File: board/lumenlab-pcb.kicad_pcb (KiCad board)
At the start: 2 copper layers, 59 parts, among them J1 2.1mm Barrel Jack, J2 Screw_Terminal_01x04, J3 Screw_Terminal_01x06, J4 Conn_01x04_Pin, U1 MP2338, U2 AP7361C-33E, U3 SN74AHC1G125DBVR, U4 1_Custom_LM386MX-1_NOPB, U5 SN74HC14DR, U6 ESP32-WROOM-32E

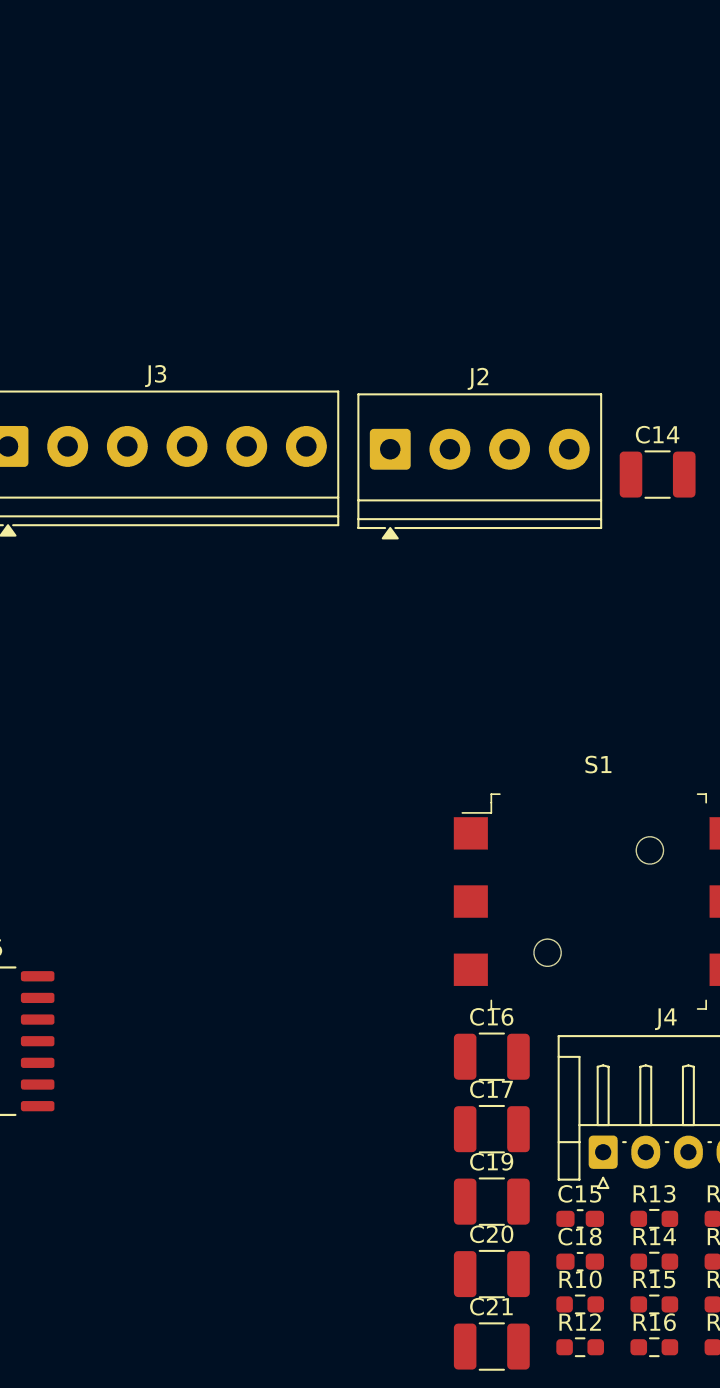
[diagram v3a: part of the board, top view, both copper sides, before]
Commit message: Add JTAG header for code upload
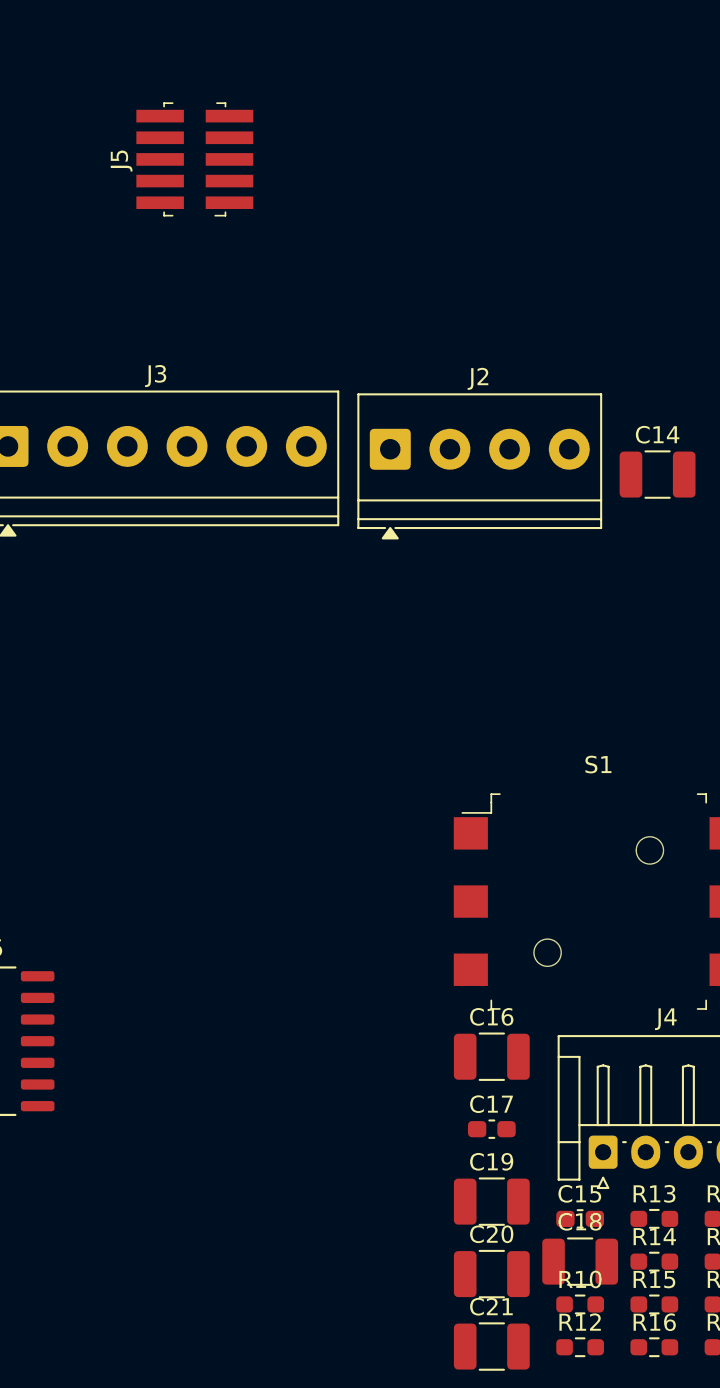
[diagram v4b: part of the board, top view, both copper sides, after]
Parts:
- added J5: JTAG, digikey-footprints:PinHeader_2x5_P1.27_SMD, F.Cu at (180.0, 69.5)
- C11: value 0.1uF -> 22uF
- C12: value 10uF -> 0.1uF
- C17: footprint Capacitor_SMD:C_1210_3225Metric_Pad1.33x2.70mm_HandSolder -> Capacitor_SMD:C_0603_1608Metric_Pad1.08x0.95mm_HandSolder
- C18: footprint Capacitor_SMD:C_0603_1608Metric_Pad1.08x0.95mm_HandSolder -> Capacitor_SMD:C_1210_3225Metric_Pad1.33x2.70mm_HandSolder
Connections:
- C11 pad 1: /DEBOUNCE_UP -> GND
- C11 pad 2: GND -> +3.3V
- C12 pad 1: GND -> +3.3V
- C12 pad 2: +3.3V -> GND
- C14 pad 1: +3.3V -> /DEBOUNCE_UP
- C17 pad 1: /DEBOUNCE_DOWN -> GND
- C17 pad 2: GND -> +3.3V
- C18 pad 1: GND -> /DEBOUNCE_DOWN
- C18 pad 2: +3.3V -> GND
- R18 pad 1: /ESP32_GPIO21 -> /ESP32_GPIO19
- S1 pad 2: GND -> /DEBOUNCE_LEFT
- S1 pad 3: GND -> /DEBOUNCE_PUSH
- S1 pad 4: GND -> /DEBOUNCE_UP
- S1 pad 5: GND -> /DEBOUNCE_RIGHT
- S1 pad 6: GND -> /DEBOUNCE_DOWN
- U6 pad 31: unconnected-(U6-IO19-Pad31) -> /ESP32_GPIO19
- U6 pad 36: unconnected-(U6-IO22-Pad36) -> /ESP32_GPIO22

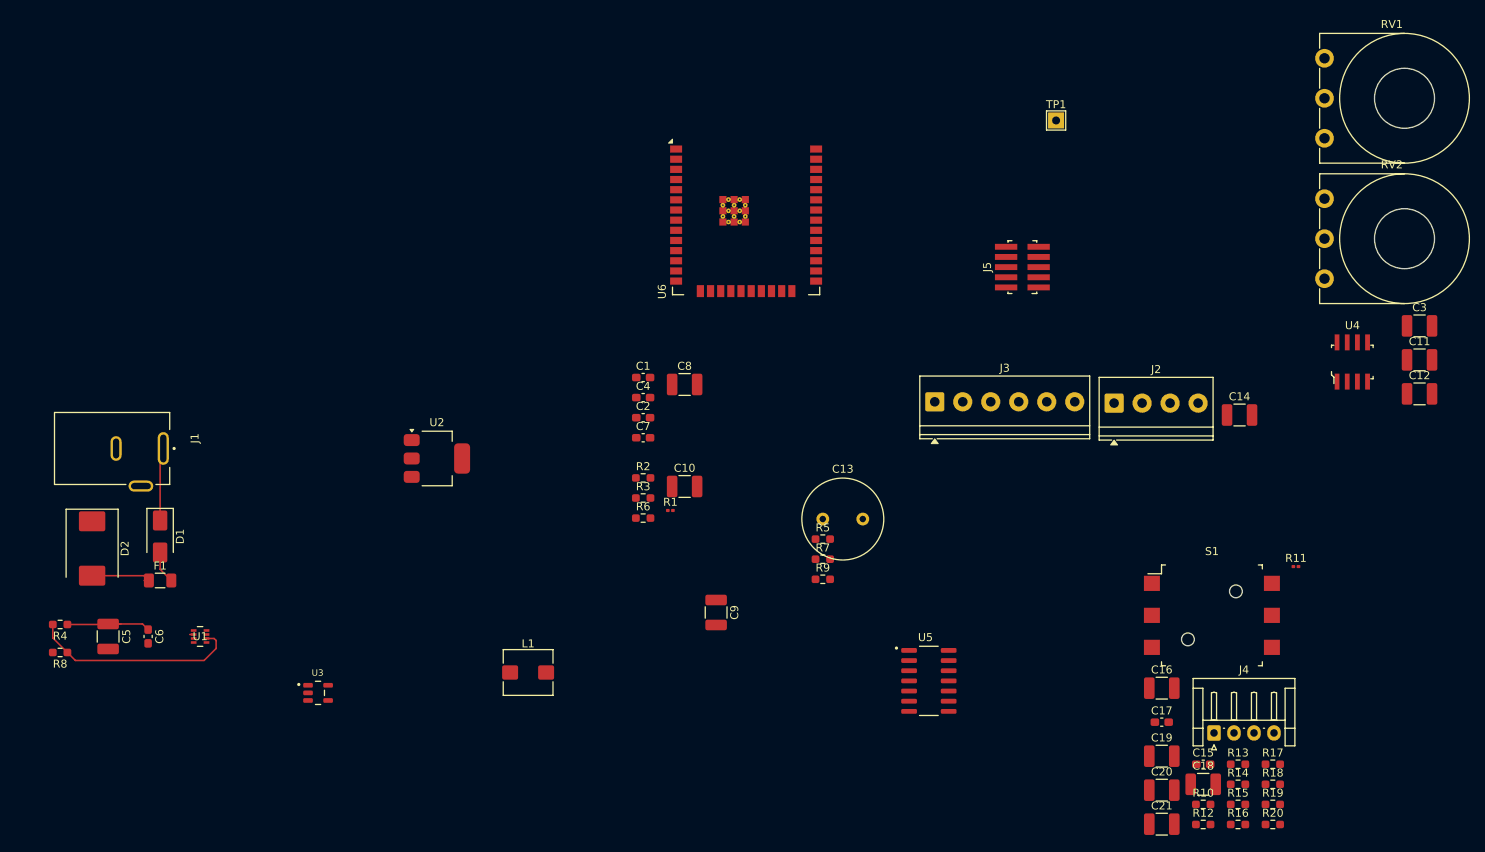
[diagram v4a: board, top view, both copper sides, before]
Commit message: Replace footprints with available components, add models
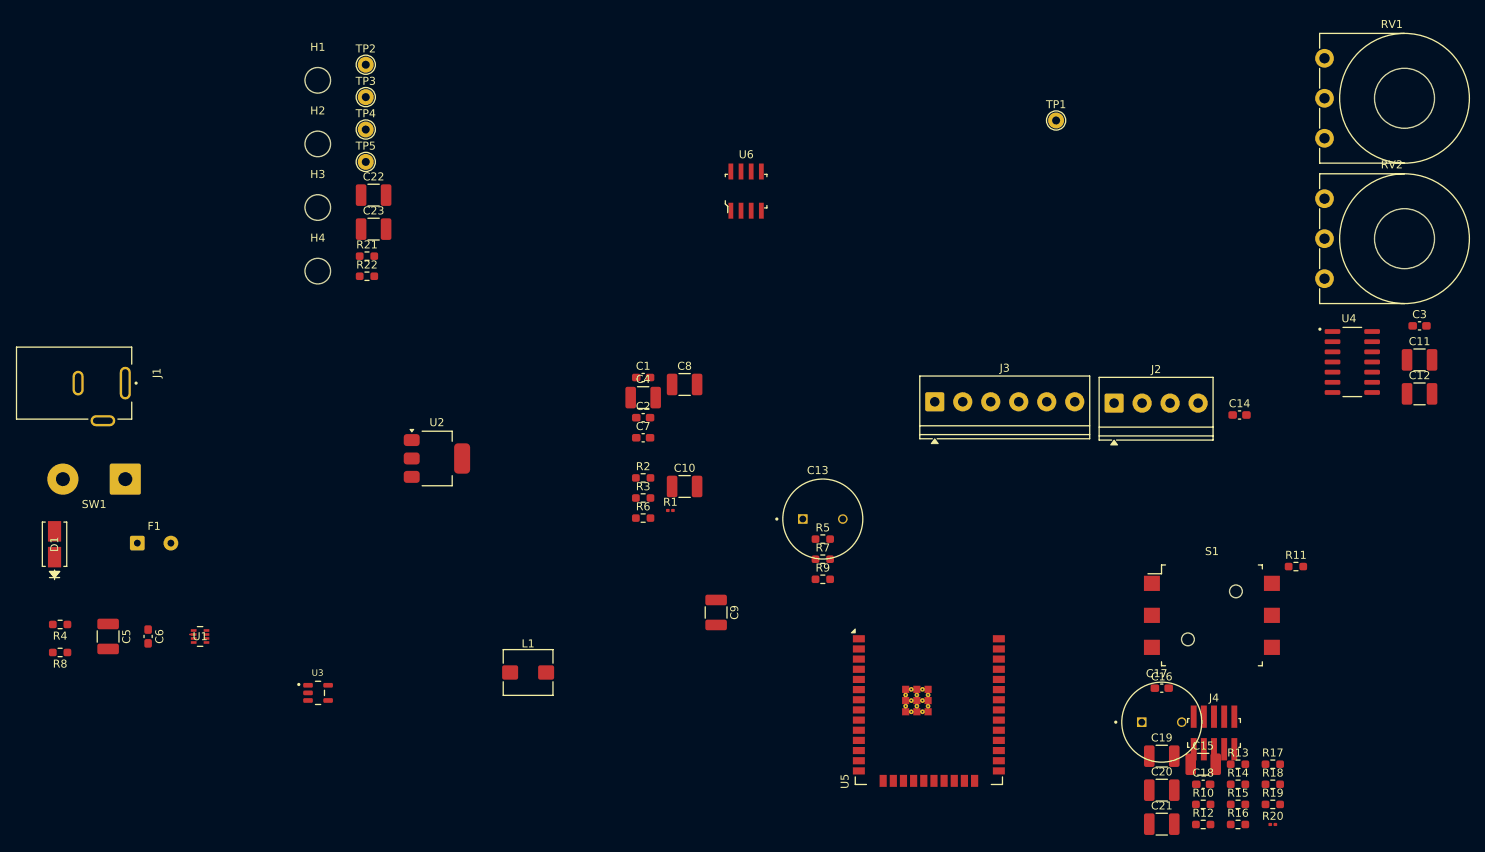
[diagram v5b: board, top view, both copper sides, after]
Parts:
- removed D2: ~, Diode_SMD:D_SMC
- removed J5: JTAG, digikey-footprints:PinHeader_2x5_P1.27_SMD
- added C22: 0.1uF, Capacitor_SMD:C_1210_3225Metric_Pad1.33x2.70mm_HandSolder, F.Cu at (98.9, 60.5)
- added C23: 0.1uF, Capacitor_SMD:C_1210_3225Metric_Pad1.33x2.70mm_HandSolder, F.Cu at (98.9, 64.8)
- added H1: MountingHole, MountingHole:MountingHole_3.2mm_M3, F.Cu at (92.0, 46.1)
- added H2: MountingHole, MountingHole:MountingHole_3.2mm_M3, F.Cu at (92.0, 54.1)
- added H3: MountingHole, MountingHole:MountingHole_3.2mm_M3, F.Cu at (92.0, 62.0)
- added H4: MountingHole, MountingHole:MountingHole_3.2mm_M3, F.Cu at (92.0, 70.0)
- added R21: 1K, Resistor_SMD:R_0603_1608Metric_Pad0.98x0.95mm_HandSolder, F.Cu at (98.1, 68.1)
- added R22: 47K, Resistor_SMD:R_0603_1608Metric_Pad0.98x0.95mm_HandSolder, F.Cu at (98.1, 70.6)
- added SW1: SW_SPST, Connector_Wire:SolderWire-1sqmm_1x02_P7.8mm_D1.4mm_OD3.9mm, F.Cu at (67.9, 96.0)
- added TP2: TestPoint, TestPoint:TestPoint_THTPad_D2.0mm_Drill1.0mm, F.Cu at (98.0, 44.2)
- added TP3: TestPoint, TestPoint:TestPoint_THTPad_D2.0mm_Drill1.0mm, F.Cu at (98.0, 48.2)
- added TP4: TestPoint, TestPoint:TestPoint_THTPad_D2.0mm_Drill1.0mm, F.Cu at (98.0, 52.3)
- added TP5: TestPoint, TestPoint:TestPoint_THTPad_D2.0mm_Drill1.0mm, F.Cu at (98.0, 56.4)
- C13: footprint Capacitor_THT:C_Radial_D10.0mm_H20.0mm_P5.00mm -> 2_Vendor_16SEPF:CAPPRD500W60D1000H1300
- C14, C18, C3: footprint Capacitor_SMD:C_1210_3225Metric_Pad1.33x2.70mm_HandSolder -> Capacitor_SMD:C_0603_1608Metric_Pad1.08x0.95mm_HandSolder
- C15, C4: footprint Capacitor_SMD:C_0603_1608Metric_Pad1.08x0.95mm_HandSolder -> Capacitor_SMD:C_1210_3225Metric_Pad1.33x2.70mm_HandSolder
- C16: value 0.05uF -> 0.1uF; footprint Capacitor_SMD:C_1210_3225Metric_Pad1.33x2.70mm_HandSolder -> Capacitor_SMD:C_0603_1608Metric_Pad1.08x0.95mm_HandSolder
- C17: value 0.1uF -> 1000uF; footprint Capacitor_SMD:C_0603_1608Metric_Pad1.08x0.95mm_HandSolder -> 2_Vendor_16SEPF:CAPPRD500W60D1000H1300
- C21: value 0.1uF -> 0.05uF
- D1: value SS34 -> SMAJ12CA; footprint Diode_SMD:D_SMA -> 2_Vendor_SMAJ12CA:SMASeries_LTF-M
- F1: footprint Fuse:Fuse_1206_3216Metric -> Connector_Wire:SolderWire-0.25sqmm_1x02_P4.2mm_D0.65mm_OD1.7mm
- J4: value Conn_01x04_Pin -> JTAG; footprint Connector_JST:JST_EH_S4B-EH_1x04_P2.50mm_Horizontal -> digikey-footprints:PinHeader_2x5_P1.27_SMD
- R10: value 47K -> 10K
- R11: value 90.9K -> 10K; footprint Resistor_SMD:R_0201_0603Metric -> Resistor_SMD:R_0603_1608Metric_Pad0.98x0.95mm_HandSolder
- R12: value 100 -> 47K
- R13: value 47K -> 100
- R16: value 1K -> 47K
- R20: value 47K -> 90.9K; footprint Resistor_SMD:R_0603_1608Metric_Pad0.98x0.95mm_HandSolder -> Resistor_SMD:R_0201_0603Metric
- RV1: value 10K LIN -> 10K LOG
- RV2: value 10K LOG -> 10K LIN
- TP1: footprint TestPoint:TestPoint_THTPad_2.0x2.0mm_Drill1.0mm -> TestPoint:TestPoint_THTPad_D2.0mm_Drill1.0mm
- U3: value SN74AHC1G125DBVR -> SN74AHCT1G125; footprint 2_Vendor_SN74AHC1G125:SN74AHC1G125 -> 2_Vendor_SN74AHCT1G125:SOT95P280X145-5N
- U4: value 1_Custom_LM386MX-1_NOPB -> SN74HC14DR; footprint digikey-footprints:SOIC-8_W3.9mm -> 2_Vendor_SN74HC14N:sn74hc14dr
- U5: value SN74HC14DR -> ESP32-WROOM-32E; footprint 2_Vendor_SN74HC14N:sn74hc14dr -> RF_Module:ESP32-WROOM-32E
- U6: value ESP32-WROOM-32E -> 1_Custom_LM386MX-1_NOPB; footprint RF_Module:ESP32-WROOM-32E -> digikey-footprints:SOIC-8_W3.9mm
- moved D1 13.2 mm to (59.1, 104.1), turned to 90 degrees
- moved J1 9.45 mm to (62.0, 84.0)
- moved F1 5.47 mm to (69.4, 104.0)
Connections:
- C14 pad 1: /DEBOUNCE_UP -> +12V
- C15 pad 1: +12V -> /DEBOUNCE_UP
- C16 pad 1: Net-(C16-Pad1) -> +12V
- C16 pad 2: Net-(C16-Pad2) -> GND
- C17 pad 1: GND -> +12V
- C17 pad 2: +3.3V -> GND
- C18 pad 1: /DEBOUNCE_DOWN -> GND
- C18 pad 2: GND -> +3.3V
- C19 pad 1: /DEBOUNCE_LEFT -> /DEBOUNCE_DOWN
- C20 pad 1: /DEBOUNCE_RIGHT -> /DEBOUNCE_LEFT
- C21 pad 1: /DEBOUNCE_PUSH -> Net-(C21-Pad1)
- C21 pad 2: GND -> Net-(C21-Pad2)
- C3 pad 1: Net-(U3-VCC) -> /BUCK_BST
- C3 pad 2: +5V -> /BUCK_SW
- C4 pad 1: /BUCK_BST -> GND
- C4 pad 2: /BUCK_SW -> +5V
- D1 pad 1: +12V -> GND
- D1 pad 2: Net-(D1-A) -> /FUSE
- F1 pad 1: +12V -> /FUSE
- F1 pad 2: Net-(D1-A) -> +12V
- J1 pad 1: +12V -> Net-(SW1-A)
- J4 pad 1: unconnected-(J4-Pin_1-Pad1) -> +3.3V
- J4 pad 2: unconnected-(J4-Pin_2-Pad2) -> /ESP32_GPIO14
- J4 pad 3: unconnected-(J4-Pin_3-Pad3) -> GND
- J4 pad 4: unconnected-(J4-Pin_4-Pad4) -> /ESP32_GPIO13
- R10 pad 2: /DEBOUNCE_DOWN -> Net-(U5-EN)
- R11 pad 1: GND -> +3.3V
- R11 pad 2: Net-(C16-Pad2) -> Net-(U5-IO0)
- R12 pad 1: /ESP32_GPIO32 -> +3.3V
- R12 pad 2: Net-(U5-1Y) -> /DEBOUNCE_DOWN
- R13 pad 1: +3.3V -> /ESP32_GPIO32
- R13 pad 2: /DEBOUNCE_LEFT -> Net-(U4-1Y)
- R14 pad 2: Net-(U5-5Y) -> Net-(U4-5Y)
- R15 pad 2: Net-(U5-2Y) -> Net-(U4-2Y)
- R16 pad 1: /ESP32_GPIO34 -> +3.3V
- R16 pad 2: Net-(R16-Pad2) -> /DEBOUNCE_LEFT
- R17 pad 1: Net-(U5-4Y) -> Net-(U4-4Y)
- R18 pad 2: Net-(U5-3Y) -> Net-(U4-3Y)
- R20 pad 1: +3.3V -> GND
- R20 pad 2: /DEBOUNCE_PUSH -> Net-(C21-Pad2)
- RV1 pad 2: Net-(R16-Pad2) -> /AMP_IN
- RV1 pad 3: +3.3V -> /ESP32_GPIO25
- RV2 pad 2: /AMP_IN -> Net-(R21-Pad2)
- RV2 pad 3: /ESP32_GPIO25 -> +3.3V
- TP1 pad 1: unconnected-(TP1-Pad1) -> Net-(U5-EN)
- U3 pad 5: Net-(U3-VCC) -> +5V
- U4 pad 1: unconnected-(U4-Pad1) -> /DEBOUNCE_UP
- U4 pad 2: GND -> Net-(U4-1Y)
- U4 pad 3: /AMP_IN -> /DEBOUNCE_DOWN
- U4 pad 4: GND -> Net-(U4-2Y)
- U4 pad 5: Net-(C16-Pad1) -> /DEBOUNCE_LEFT
- U4 pad 6: +5V -> Net-(U4-3Y)
- U4 pad 7: unconnected-(U4-Pad7) -> GND
- U4 pad 8: unconnected-(U4-Pad8) -> Net-(U4-4Y)
- U5 pad 1: /DEBOUNCE_UP -> GND
- U5 pad 10: Net-(U5-5Y) -> /ESP32_GPIO25
- U5 pad 11: /DEBOUNCE_PUSH -> unconnected-(U5-IO26-Pad11)
- U5 pad 12: unconnected-(U5-6Y-Pad12) -> /ESP32_GPIO27
- U5 pad 13: GND -> /ESP32_GPIO14
- U5 pad 14: +3.3V -> /ESP32_GPIO12
- U5 pad 2: Net-(U5-1Y) -> +3.3V
- U5 pad 3: /DEBOUNCE_DOWN -> Net-(U5-EN)
- U5 pad 4: Net-(U5-2Y) -> unconnected-(U5-SENSOR_VP-Pad4)
- U5 pad 5: /DEBOUNCE_LEFT -> unconnected-(U5-SENSOR_VN-Pad5)
- U5 pad 6: Net-(U5-3Y) -> /ESP32_GPIO34
- U5 pad 7: GND -> /ESP32_GPIO35
- U5 pad 8: Net-(U5-4Y) -> /ESP32_GPIO32
- U5 pad 9: /DEBOUNCE_RIGHT -> /ESP32_GPIO33
- U6 pad 1: GND -> unconnected-(U6-Pad1)
- U6 pad 2: +3.3V -> GND
- U6 pad 3: unconnected-(U6-EN-Pad3) -> /AMP_IN
- U6 pad 4: unconnected-(U6-SENSOR_VP-Pad4) -> GND
- U6 pad 5: unconnected-(U6-SENSOR_VN-Pad5) -> Net-(C21-Pad1)
- U6 pad 6: /ESP32_GPIO34 -> +5V
- U6 pad 7: /ESP32_GPIO35 -> unconnected-(U6-Pad7)
- U6 pad 8: /ESP32_GPIO32 -> unconnected-(U6-Pad8)
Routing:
- net +12V: track 29.6 -> 0.63 mm
- net /BUCK_EN: track 26.2 -> 0.00 mm
- net Net-(D1-A): track 4.08 -> 0.00 mm

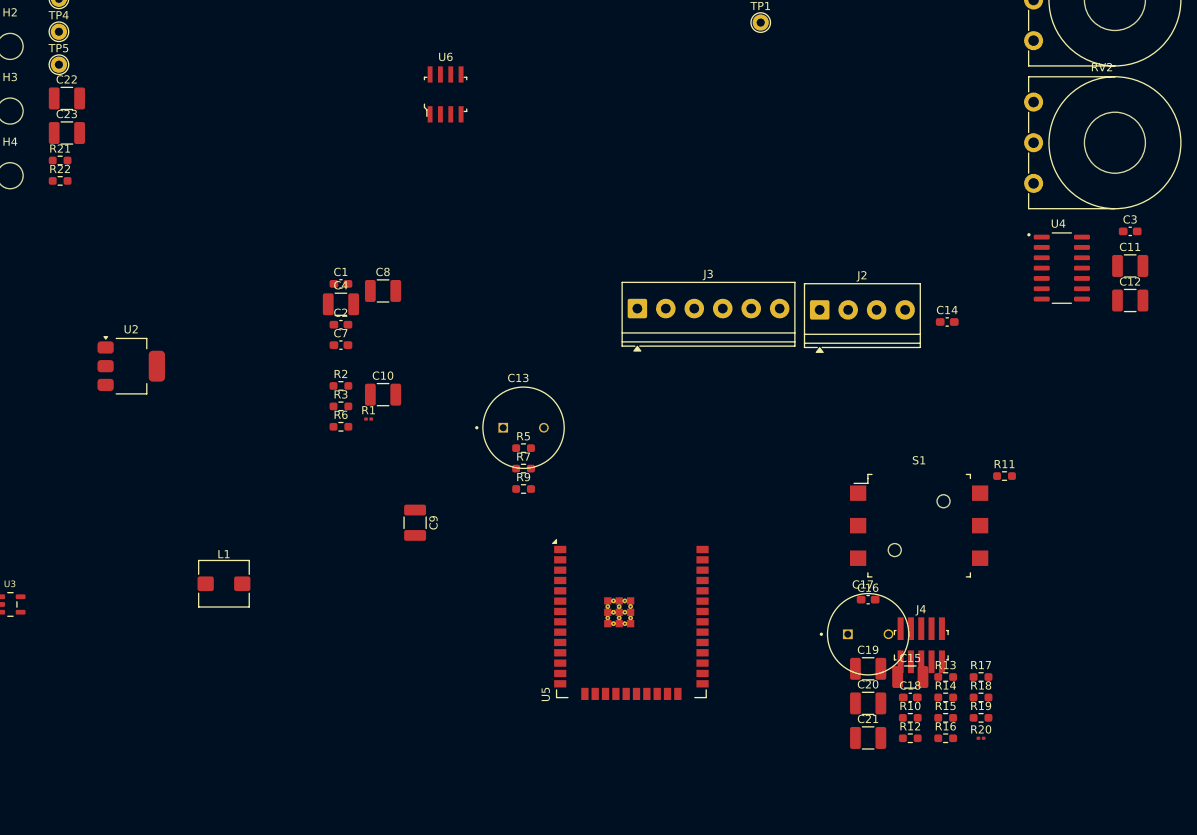
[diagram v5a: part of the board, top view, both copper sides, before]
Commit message: Continue making footprint changes, BOM additions
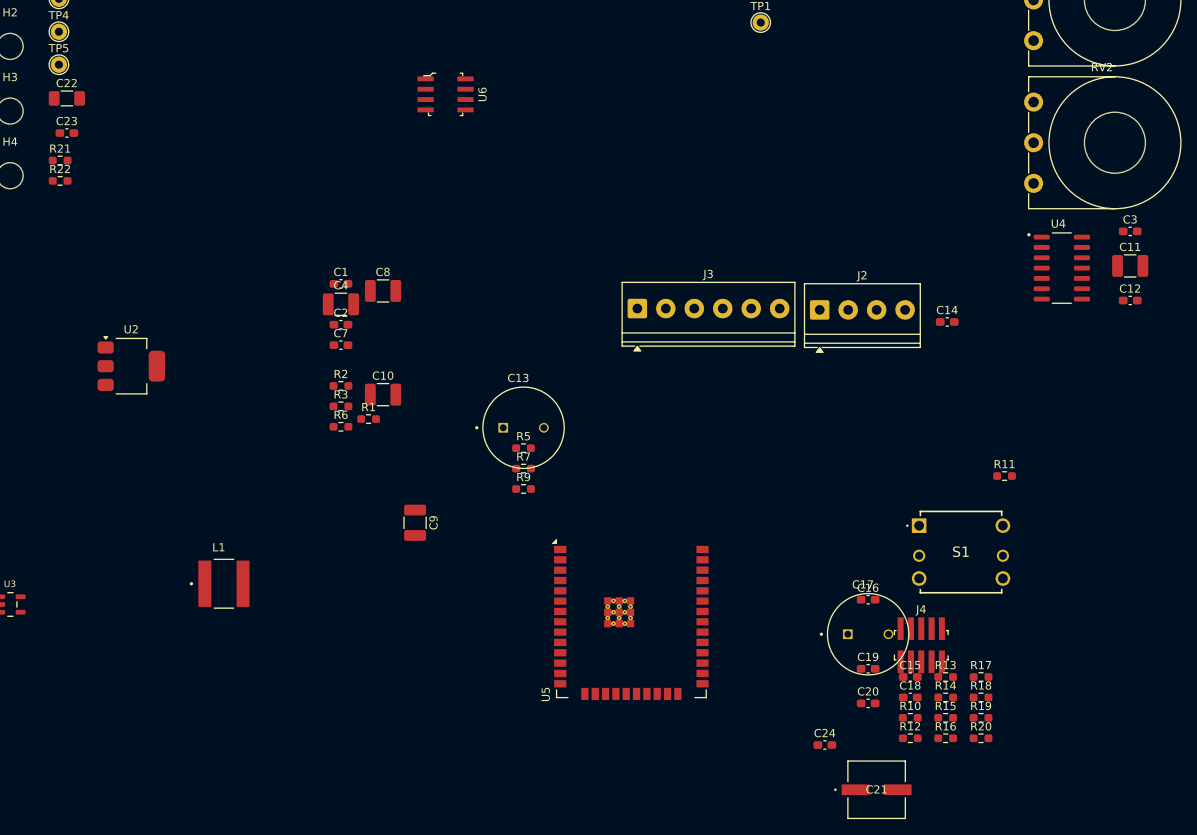
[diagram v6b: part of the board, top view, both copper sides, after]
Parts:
- added C24: 0.1uF, Capacitor_SMD:C_0603_1608Metric_Pad1.08x0.95mm_HandSolder, F.Cu at (192.1, 140.0)
- C12, C15, C19, C20, C23: footprint Capacitor_SMD:C_1210_3225Metric_Pad1.33x2.70mm_HandSolder -> Capacitor_SMD:C_0603_1608Metric_Pad1.08x0.95mm_HandSolder
- C21: value 0.05uF -> 250uF; footprint Capacitor_SMD:C_1210_3225Metric_Pad1.33x2.70mm_HandSolder -> 2_Vendor_10TZV220M6:CAP_J-V_6P3X8_RUB-M
- C22: value 0.1uF -> 0.05uF; footprint Capacitor_SMD:C_1210_3225Metric_Pad1.33x2.70mm_HandSolder -> Capacitor_SMD:C_1206_3216Metric_Pad1.33x1.80mm_HandSolder
- L1: footprint Inductor_SMD:L_Bourns_SRP5030T -> 2_Vendor_1264EY:IND_1264EY-6R8M=P3
- R1: footprint Resistor_SMD:R_0201_0603Metric -> Resistor_SMD:R_0603_1608Metric_Pad0.98x0.95mm_HandSolder
- R20: value 90.9K -> 10; footprint Resistor_SMD:R_0201_0603Metric -> Resistor_SMD:R_0603_1608Metric_Pad0.98x0.95mm_HandSolder
- S1: footprint digikey-footprints:Switch_Nav_12.4x12.4mm_SMD_JS5208 -> 2_Vendor_NavSwitch:504-nav-switch
- moved C21 6.45 mm to (198.5, 145.5)
- turned U6 to -90 degrees
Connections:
- C22 pad 1: /DEBOUNCE_RIGHT -> Net-(C21-Pad1)
- C22 pad 2: GND -> Net-(C22-Pad2)
- C23 pad 1: /DEBOUNCE_PUSH -> /DEBOUNCE_RIGHT
- R20 pad 2: Net-(C21-Pad2) -> Net-(C22-Pad2)
